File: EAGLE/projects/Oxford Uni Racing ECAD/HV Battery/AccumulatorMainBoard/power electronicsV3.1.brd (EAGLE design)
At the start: 167.6 x 103.8 mm, 97 parts, among them IC1 4043D, IC2 SE555D, IC3 4011D, IC5 4043D, IC6 4011D, IC7 4011D, IC8 4011D, IC9 4011D, K1 T9AS1D12-48=T9A, K2 T9AS5D12-12=T9A, K3 T9AS1D12-48=T9A, K4 T9AS1D12-48=T9A, Q1 BSS138, Q2 BSS138, Q3 BSS138, Q4 BSS138

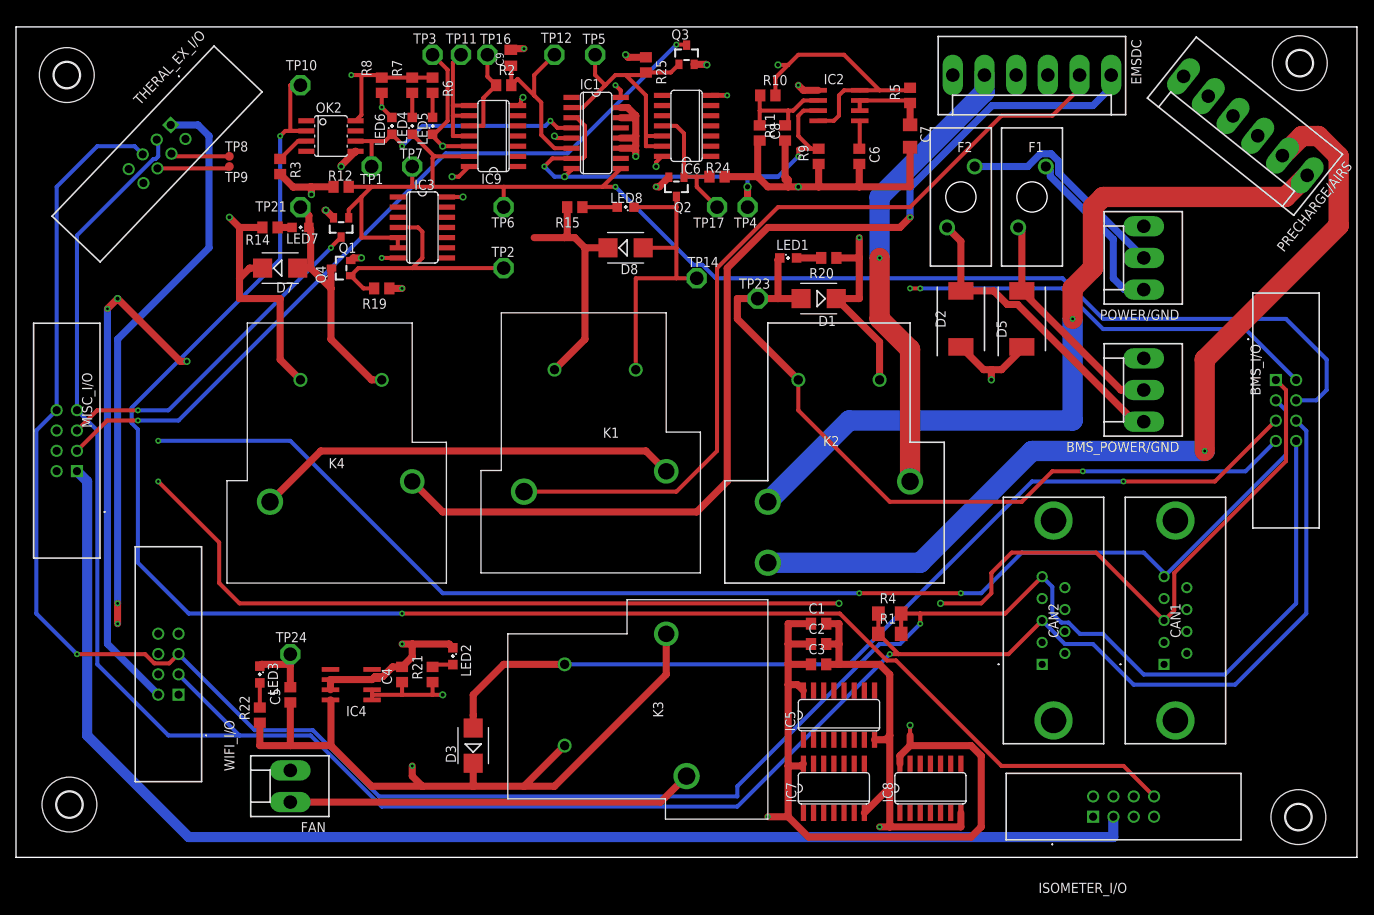
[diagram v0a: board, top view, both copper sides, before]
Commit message: Main Board V4.1
Moves some of the IC to the bottom layer. More optimal Connector placement
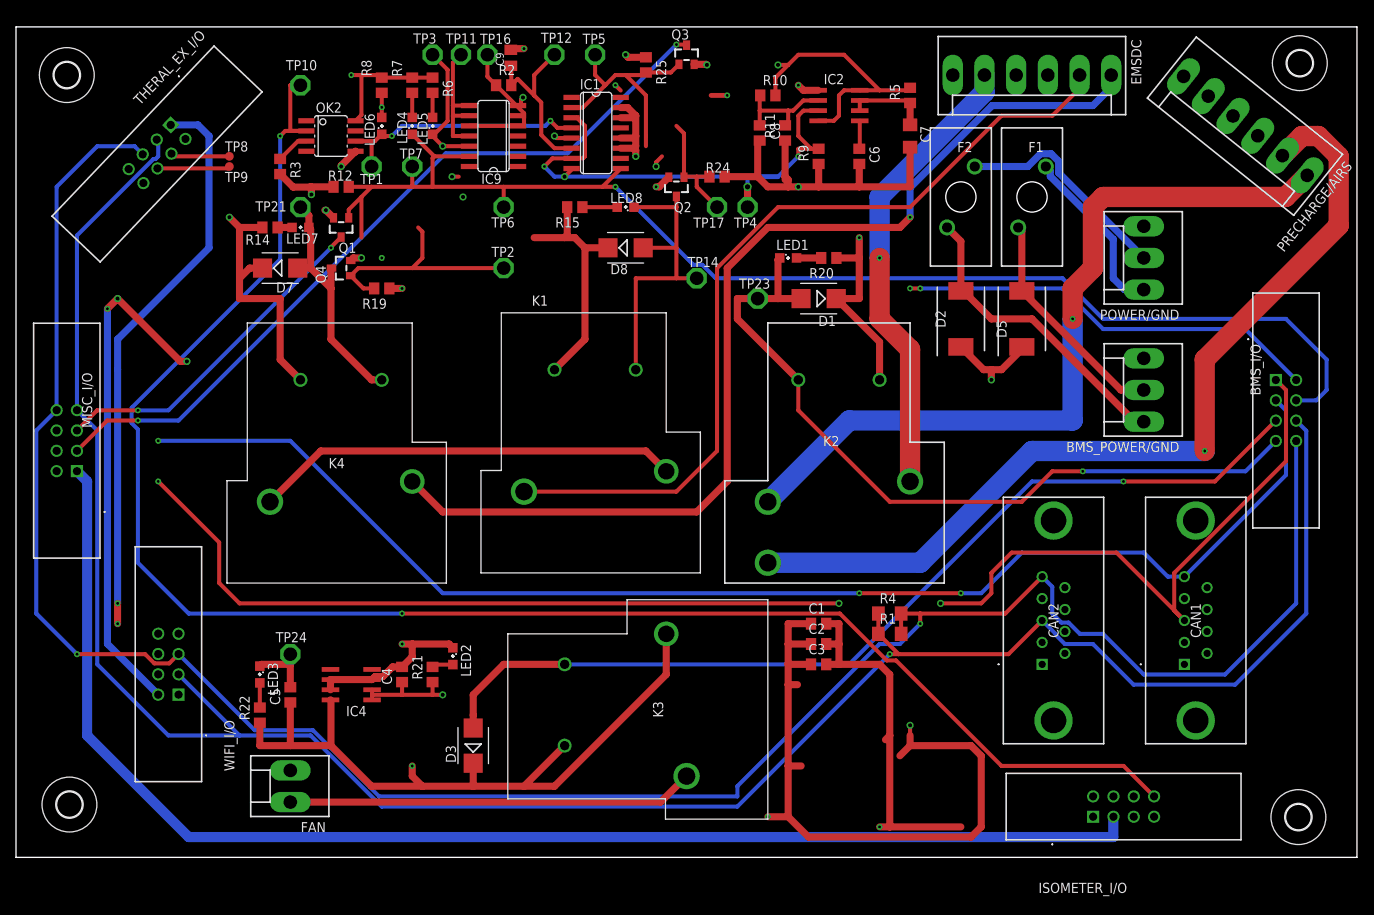
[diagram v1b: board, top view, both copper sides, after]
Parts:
- removed IC3, IC6, IC7, IC8: 4011D, 40xx:SO14
- removed IC5: 4043D, 40xx:SO16
- moved CAN1 2.54 mm to (146.1, 24.1)
- moved LED6 1.27 mm to (45.7, 91.4)
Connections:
- removed net VDD: IC1.16, IC3.14, IC6.14, IC9.14
- removed net VSS: IC1.8, IC3.7, IC6.7, IC9.7
- net +3V3: now also IC1.16, IC9.14; no longer IC5.16, IC7.14, IC8.14
- net DISCHARGE_ENABLE: now also IC9.5, IC9.6; no longer IC3.5, IC3.6
- net GND: now also IC1.8, IC9.7; no longer IC5.8, IC7.7, IC8.7
- net N$16: now also IC9.4; no longer IC3.4
- net N$8: now also IC9.3; no longer IC6.11
- net N$9: now also IC9.1, IC9.2; no longer IC6.12, IC6.13
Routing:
- net GND: track 168.3 -> 160.7 mm
- net N$1: track 11.8 -> 17.7 mm
- net DISCHARGE_ENABLE: track 175.7 -> 169.9 mm
- net VDD: track 88.1 -> 83.4 mm
- net N$9: track 34.0 -> 29.9 mm
- net VSS: track 89.6 -> 87.0 mm
- net CAN1_H: track 193.9 -> 196.4 mm
- net N$16: track 31.5 -> 28.9 mm
- net +3V3: track 180.9 -> 178.5 mm
- net N$8: track 16.7 -> 14.9 mm
- net CAN1_L: track 180.3 -> 181.5 mm
- net N$5: track 33.0 -> 31.8 mm
- net N$27: track 3.61 -> 3.08 mm
